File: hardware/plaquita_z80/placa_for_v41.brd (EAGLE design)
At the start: 37.1 x 30.4 mm, 8 parts, among them IC2 REG1117

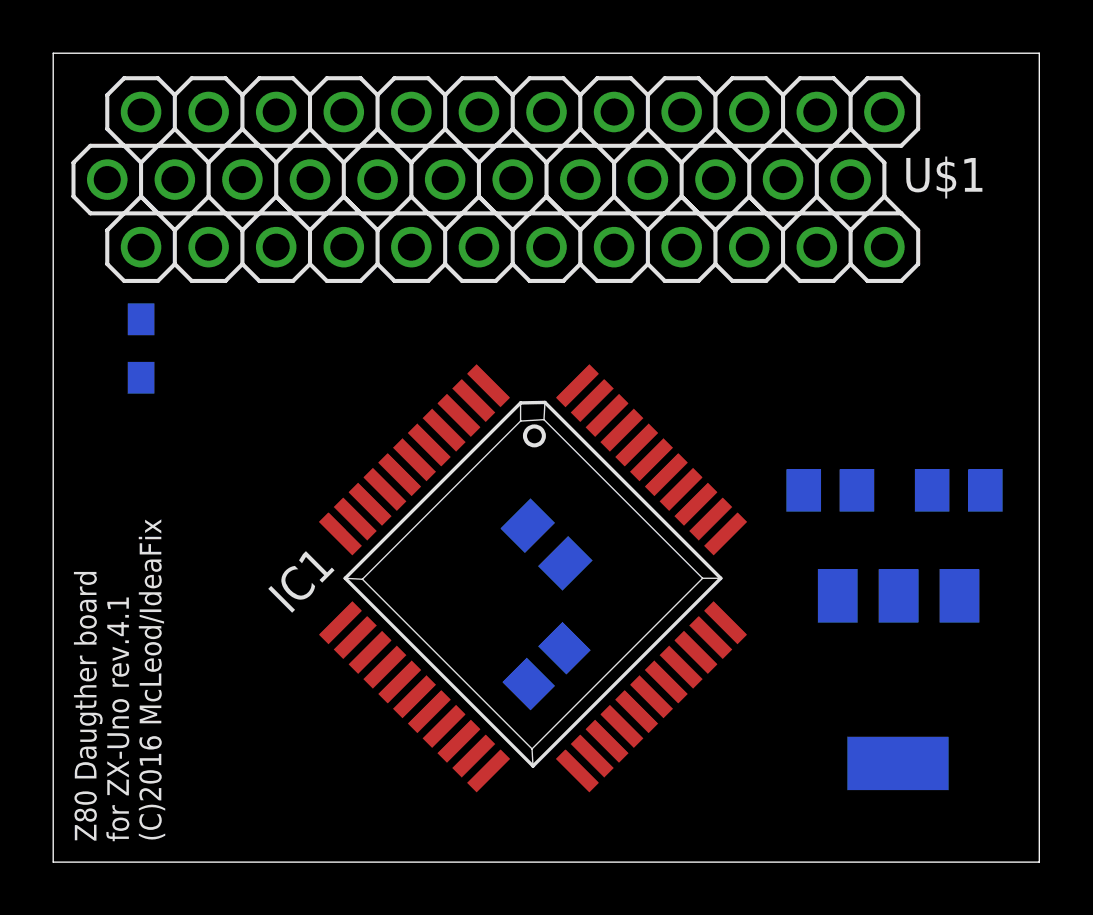
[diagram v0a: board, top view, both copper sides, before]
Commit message: 
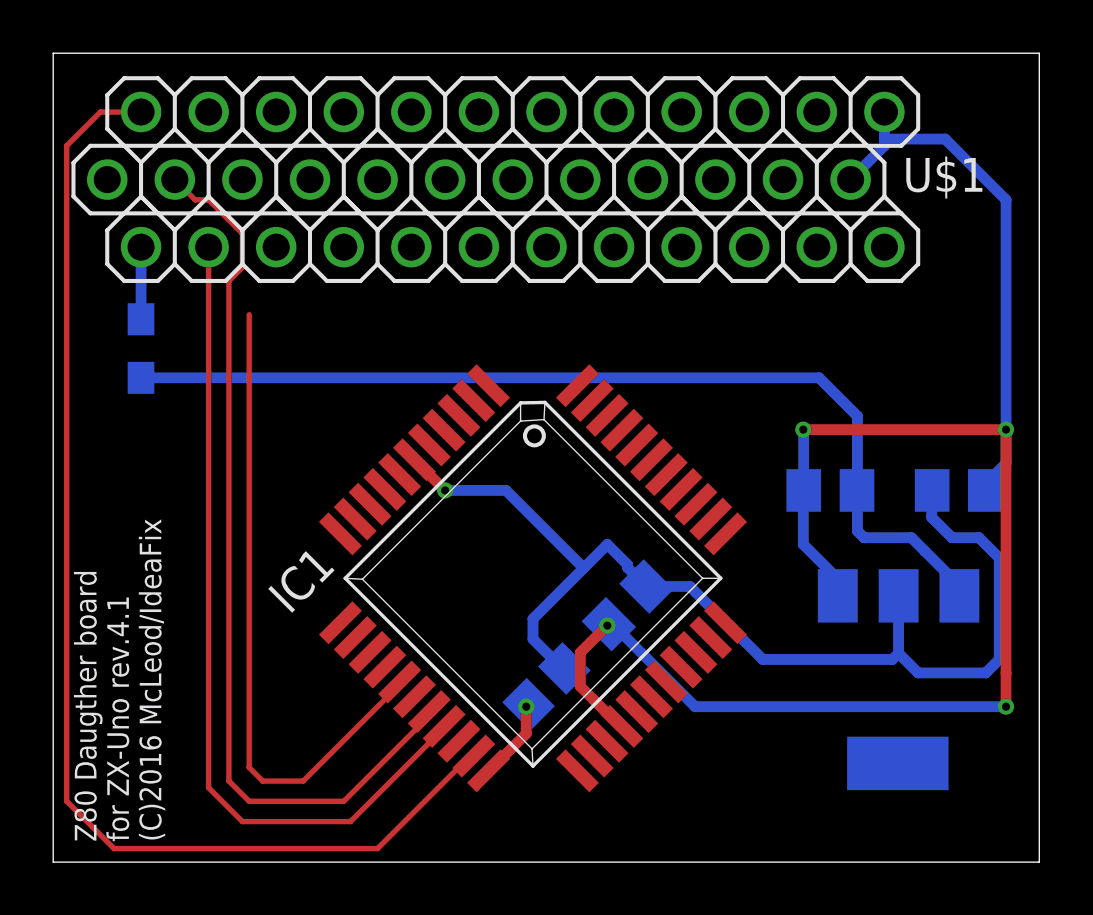
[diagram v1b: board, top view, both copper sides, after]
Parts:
- moved C1 3.81 mm to (21.6, 9.65), turned to 315 degrees
- moved R3 0.76 mm to (18.5, 6.60)
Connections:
- net /IORQ: now also U$1.P9
- net /MREQ: now also U$1.P10
- net /RD: now also U$1.P8
- net /WAIT: now also U$1.P6
- net /WR: now also U$1.P7
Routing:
- net GND: track 0.00 -> 65.8 mm, vias 0 -> 4
- net /WAIT: track 0.00 -> 45.4 mm
- net 3.3V: track 0.00 -> 41.8 mm, vias 0 -> 1
- net +5V: track 0.00 -> 36.9 mm
- net /RD: track 0.00 -> 33.5 mm
- net /WR: track 0.00 -> 31.2 mm
- net /IORQ: track 0.00 -> 24.5 mm
- net /BUSREQ: track 0.00 -> 3.14 mm, vias 0 -> 1
- net N$1: track 0.00 -> 2.71 mm

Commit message: 
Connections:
- net 3.3V renamed VCC
- net /IORQ: now also U$1.P7; no longer U$1.P9
- net /RD: now also U$1.P9; no longer U$1.P8
- net /WR: now also U$1.P8; no longer U$1.P7
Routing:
- net /WR: track 31.2 -> 40.3 mm
- net /IORQ: track 24.5 -> 33.2 mm
- net /RD: track 33.5 -> 40.8 mm
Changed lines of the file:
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@@
 <signal name="/WR">
 <contactref element="IC1" pad="19"/>
-<contactref element="U$1" pad="P7"/>
+<contactref element="U$1" pad="P8"/>
 <wire x1="14.69334375" y1="5.100240625" x2="14.69334375" y2="5.04134375" width="0.2032" layer="1"/>
-<wire x1="14.69334375" y1="5.04134375" x2="11.176" y2="1.524" width="0.2032" layer="1"/>
-<wire x1="11.176" y1="1.524" x2="7.112" y2="1.524" width="0.2032" layer="1"/>
-<wire x1="7.112" y1="1.524" x2="5.842" y2="2.794" width="0.2032" layer="1"/>
-<wire x1="5.842" y1="2.794" x2="5.842" y2="23.114" width="0.2032" layer="1"/>
+<wire x1="14.69334375" y1="5.04134375" x2="10.922" y2="1.27" width="0.2032" layer="1"/>
+<wire x1="10.922" y1="1.27" x2="2.794" y2="1.27" width="0.2032" layer="1"/>
+<wire x1="2.794" y1="1.27" x2="1.27" y2="2.794" width="0.2032" layer="1"/>
+<wire x1="1.27" y1="2.794" x2="1.27" y2="23.114" width="0.2032" layer="1"/>
+<wire x1="1.27" y1="23.114" x2="3.302" y2="25.146" width="0.2032" layer="1"/>
+<wire x1="3.302" y1="25.146" x2="4.064" y2="25.146" width="0.2032" layer="1"/>
+<wire x1="4.064" y1="25.146" x2="4.572" y2="25.654" width="0.2032" layer="1"/>
 </signal>
 <signal name="/RD">
 <contactref element="IC1" pad="18"/>
-<contactref element="U$1" pad="P8"/>
+<contactref element="U$1" pad="P9"/>
 <wire x1="14.13656875" y1="5.657015625" x2="14.13656875" y2="5.50056875" width="0.2032" layer="1"/>
-<wire x1="14.13656875" y1="5.50056875" x2="10.922" y2="2.286" width="0.2032" layer="1"/>
-<wire x1="10.922" y1="2.286" x2="7.366" y2="2.286" width="0.2032" layer="1"/>
-<wire x1="7.366" y1="2.286" x2="6.604" y2="3.048" width="0.2032" layer="1"/>
-<wire x1="6.604" y1="3.048" x2="6.604" y2="21.844" width="0.2032" layer="1"/>
-<wire x1="6.604" y1="21.844" x2="7.112" y2="22.352" width="0.2032" layer="1"/>
-<wire x1="7.112" y1="22.352" x2="7.112" y2="23.622" width="0.2032" layer="1"/>
-<wire x1="7.112" y1="23.622" x2="5.842" y2="24.892" width="0.2032" layer="1"/>
-<wire x1="5.842" y1="24.892" x2="5.334" y2="24.892" width="0.2032" layer="1"/>
-<wire x1="5.334" y1="24.892" x2="4.572" y2="25.654" width="0.2032" layer="1"/>
+<wire x1="14.13656875" y1="5.50056875" x2="10.668" y2="2.032" width="0.2032" layer="1"/>
+<wire x1="10.668" y1="2.032" x2="3.048" y2="2.032" width="0.2032" layer="1"/>
+<wire x1="3.048" y1="2.032" x2="2.032" y2="3.048" width="0.2032" layer="1"/>
+<wire x1="2.032" y1="3.048" x2="2.032" y2="19.812" width="0.2032" layer="1"/>
+<wire x1="2.032" y1="19.812" x2="4.572" y2="22.352" width="0.2032" layer="1"/>
+<wire x1="4.572" y1="22.352" x2="4.572" y2="23.622" width="0.2032" layer="1"/>
+<wire x1="4.572" y1="23.622" x2="5.842" y2="24.892" width="0.2032" layer="1"/>
+<wire x1="5.842" y1="24.892" x2="5.842" y2="28.194" width="0.2032" layer="1"/>
 </signal>
 <signal name="/IORQ">
 <contactref element="IC1" pad="16"/>
-<contactref element="U$1" pad="P9"/>
+<contactref element="U$1" pad="P7"/>
 <wire x1="13.023015625" y1="6.77056875" x2="13.023015625" y2="6.673015625" width="0.2032" layer="1"/>
-<wire x1="13.023015625" y1="6.673015625" x2="9.398" y2="3.048" width="0.2032" layer="1"/>
-<wire x1="9.398" y1="3.048" x2="7.874" y2="3.048" width="0.2032" layer="1"/>
-<wire x1="7.874" y1="3.048" x2="7.366" y2="3.556" width="0.2032" layer="1"/>
-<wire x1="7.366" y1="3.556" x2="7.366" y2="20.574" width="0.2032" layer="1"/>
-<wire x1="7.366" y1="20.574" x2="5.842" y2="28.194" width="0" layer="19" extent="1-16"/>
+<wire x1="13.023015625" y1="6.673015625" x2="9.144" y2="2.794" width="0.2032" layer="1"/>
+<wire x1="9.144" y1="2.794" x2="3.302" y2="2.794" width="0.2032" layer="1"/>
+<wire x1="3.302" y1="2.794" x2="2.794" y2="3.302" width="0.2032" layer="1"/>
+<wire x1="2.794" y1="3.302" x2="2.794" y2="18.796" width="0.2032" layer="1"/>
+<wire x1="2.794" y1="18.796" x2="5.842" y2="21.844" width="0.2032" layer="1"/>
+<wire x1="5.842" y1="21.844" x2="5.842" y2="23.114" width="0.2032" layer="1"/>
 </signal>
 <signal name="/MREQ">
@@
 <wire x1="1.778" y1="28.194" x2="3.302" y2="28.194" width="0.2032" layer="1"/>
 </signal>
-<signal name="3.3V" class="1">
+<signal name="VCC" class="1">
 <contactref element="IC1" pad="6"/>
 <contactref element="C1" pad="1"/>

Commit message: 
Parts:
- renumbered U$1 to CONN_ZXUNO
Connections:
- new net N$10: CONN_ZXUNO.P23
- new net N$11: CONN_ZXUNO.P24
- new net N$12: CONN_ZXUNO.P25
- new net N$13: CONN_ZXUNO.P26
- new net N$9: CONN_ZXUNO.P22
- net /INT: now also CONN_ZXUNO.P12
- net /MREQ: now also CONN_ZXUNO.P11; no longer CONN_ZXUNO.P10
- net /NMI: now also CONN_ZXUNO.P10
- net CLK: now also CONN_ZXUNO.P19
- net D0: now also CONN_ZXUNO.P13
- net D1: now also CONN_ZXUNO.P14
- net D2: now also CONN_ZXUNO.P18
- net D3: now also CONN_ZXUNO.P21
- net D4: now also CONN_ZXUNO.P20
- net D5: now also CONN_ZXUNO.P16
- net D6: now also CONN_ZXUNO.P17
- net D7: now also CONN_ZXUNO.P15
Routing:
- net /MREQ: track 0.00 -> 33.9 mm
- net /INT: track 0.00 -> 32.6 mm, vias 0 -> 1
- net /NMI: track 0.00 -> 28.9 mm
- net D2: track 0.00 -> 17.3 mm
- net D7: track 0.00 -> 15.9 mm, vias 0 -> 1
- net D3: track 0.00 -> 14.8 mm
- net D1: track 0.00 -> 14.7 mm
- net D0: track 0.00 -> 11.8 mm
- net D6: track 0.00 -> 11.5 mm, vias 0 -> 1
- net D4: track 0.00 -> 9.46 mm, vias 0 -> 1
- net D5: track 0.00 -> 8.44 mm
- net CLK: track 0.00 -> 5.36 mm
- net +5V: track 36.9 -> 39.7 mm

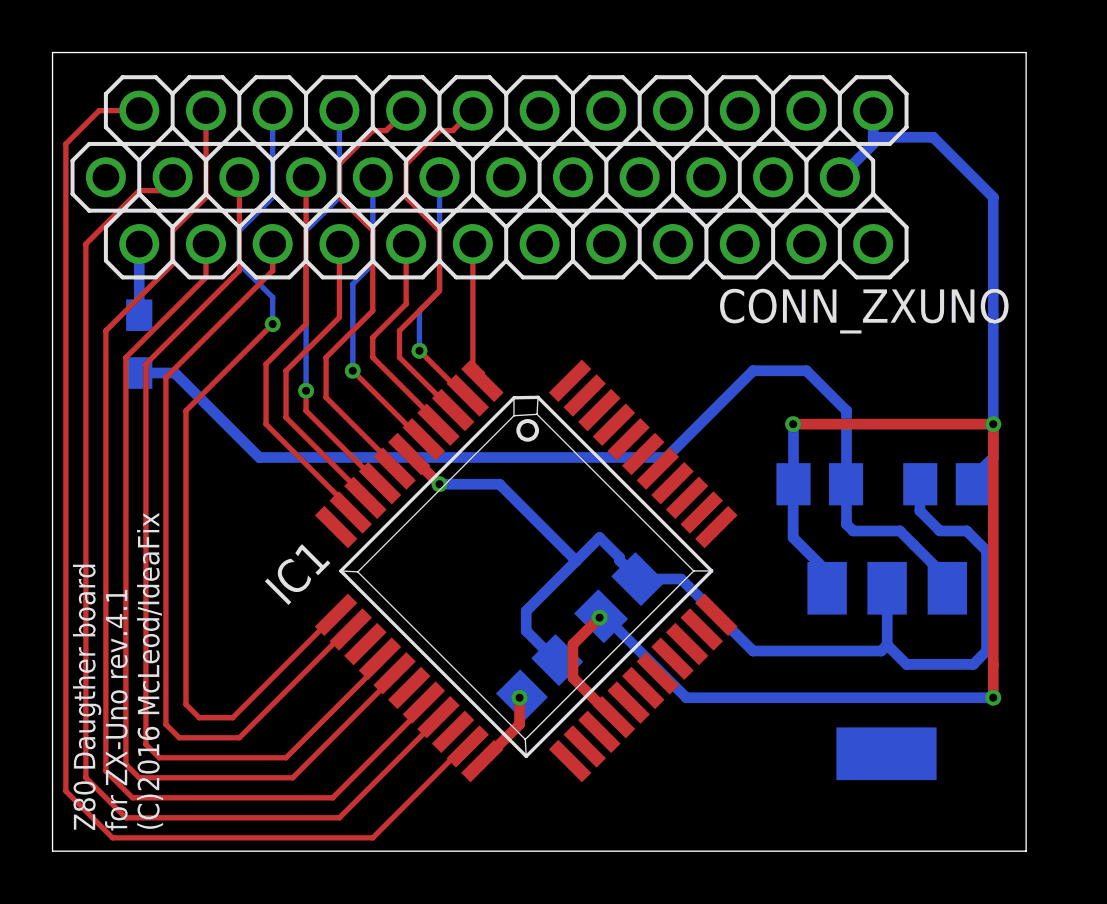
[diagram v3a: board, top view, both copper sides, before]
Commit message: 
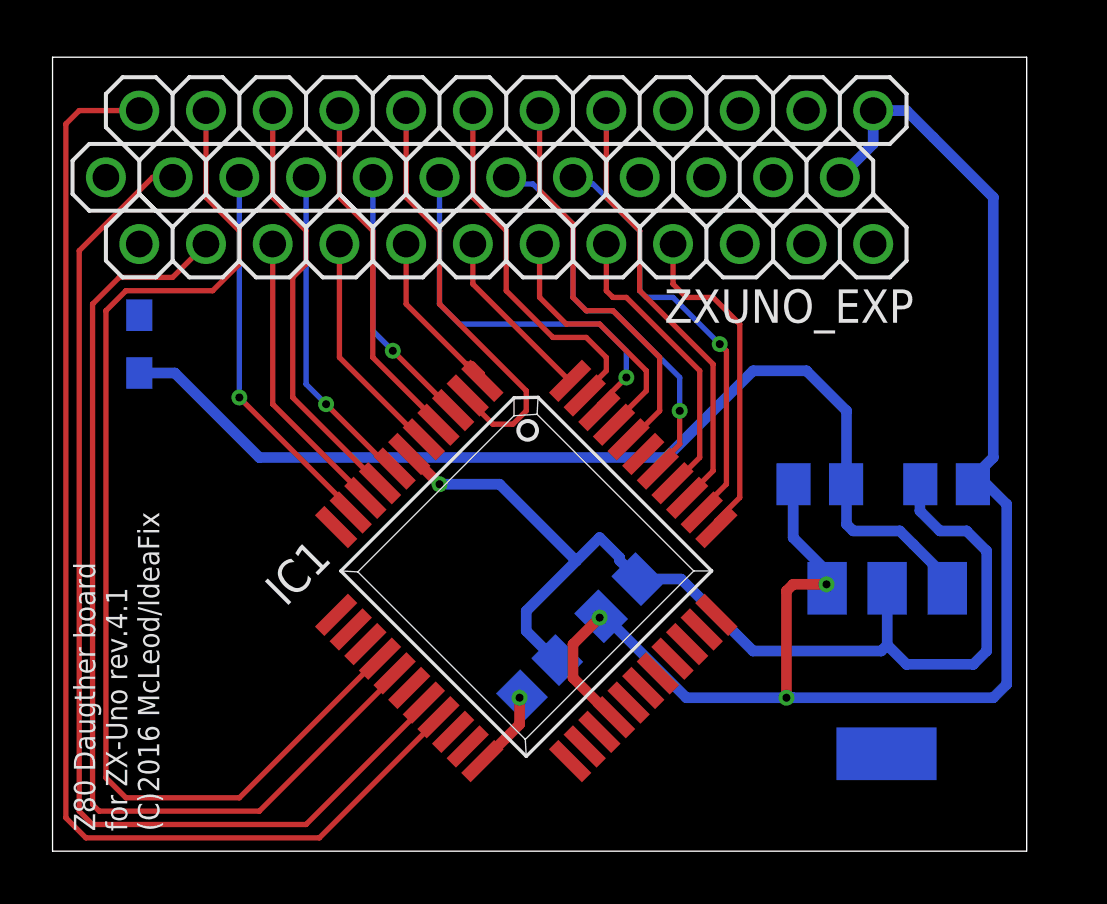
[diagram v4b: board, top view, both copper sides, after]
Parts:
- renumbered CONN_ZXUNO to ZXUNO_EXP
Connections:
- removed net N$10: ZXUNO_EXP.P23
- removed net N$11: ZXUNO_EXP.P24
- removed net N$12: ZXUNO_EXP.P25
- removed net N$13: ZXUNO_EXP.P26
- removed net N$9: ZXUNO_EXP.P22
- new net 3.3V: ZXUNO_EXP.3.3V@1, ZXUNO_EXP.3.3V@2
- new net N$18: ZXUNO_EXP.P29
- new net N$19: ZXUNO_EXP.P30
- new net N$20: ZXUNO_EXP.P31
- new net N$21: ZXUNO_EXP.P32
- new net N$22: ZXUNO_EXP.P33
- net /INT: no longer ZXUNO_EXP.P12
- net /MREQ: now also ZXUNO_EXP.P9; no longer ZXUNO_EXP.P11
- net /NMI: no longer ZXUNO_EXP.P10
- net /RD: now also ZXUNO_EXP.P8; no longer ZXUNO_EXP.P9
- net /WAIT: no longer ZXUNO_EXP.P6
- net /WR: now also ZXUNO_EXP.P6; no longer ZXUNO_EXP.P8
- net A10: now also ZXUNO_EXP.P23
- net A11: now also ZXUNO_EXP.P24
- net A12: now also ZXUNO_EXP.P22
- net A13: now also ZXUNO_EXP.P20
- net A14: now also ZXUNO_EXP.P21
- net A15: now also ZXUNO_EXP.P19
- net A6: now also ZXUNO_EXP.P28
- net A7: now also ZXUNO_EXP.P26
- net A8: now also ZXUNO_EXP.P27
- net A9: now also ZXUNO_EXP.P25
- net CLK: now also ZXUNO_EXP.P16; no longer ZXUNO_EXP.P19
- net D0: now also ZXUNO_EXP.P10; no longer ZXUNO_EXP.P13
- net D1: now also ZXUNO_EXP.P11; no longer ZXUNO_EXP.P14
- net D2: now also ZXUNO_EXP.P14; no longer ZXUNO_EXP.P18
- net D3: now also ZXUNO_EXP.P17; no longer ZXUNO_EXP.P21
- net D4: now also ZXUNO_EXP.P18; no longer ZXUNO_EXP.P20
- net D5: now also ZXUNO_EXP.P15; no longer ZXUNO_EXP.P16
- net D6: now also ZXUNO_EXP.P13; no longer ZXUNO_EXP.P17
- net D7: now also ZXUNO_EXP.P12; no longer ZXUNO_EXP.P15
- net VCC: no longer ZXUNO_EXP.3.3V@1, ZXUNO_EXP.3.3V@2
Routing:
- net /WAIT: track 45.4 -> 0.00 mm
- net /INT: track 32.6 -> 0.00 mm, vias 1 -> 0
- net /NMI: track 28.9 -> 0.00 mm
- net A8: track 0.00 -> 16.8 mm
- net A7: track 0.00 -> 16.5 mm, vias 0 -> 1
- net A11: track 0.00 -> 15.6 mm
- net A13: track 0.00 -> 15.4 mm, vias 0 -> 1
- net A10: track 0.00 -> 15.2 mm, vias 0 -> 1
- net A14: track 0.00 -> 14.0 mm
- net A6: track 0.00 -> 12.8 mm
- net A9: track 0.00 -> 11.3 mm
- net A12: track 0.00 -> 9.82 mm
- net /MREQ: track 33.9 -> 42.9 mm
- net D4: track 9.46 -> 16.5 mm, vias 1 -> 0
- net A15: track 0.00 -> 6.75 mm
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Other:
- board size 37.1 x 30.4 mm -> 37.1 x 30.2 mm

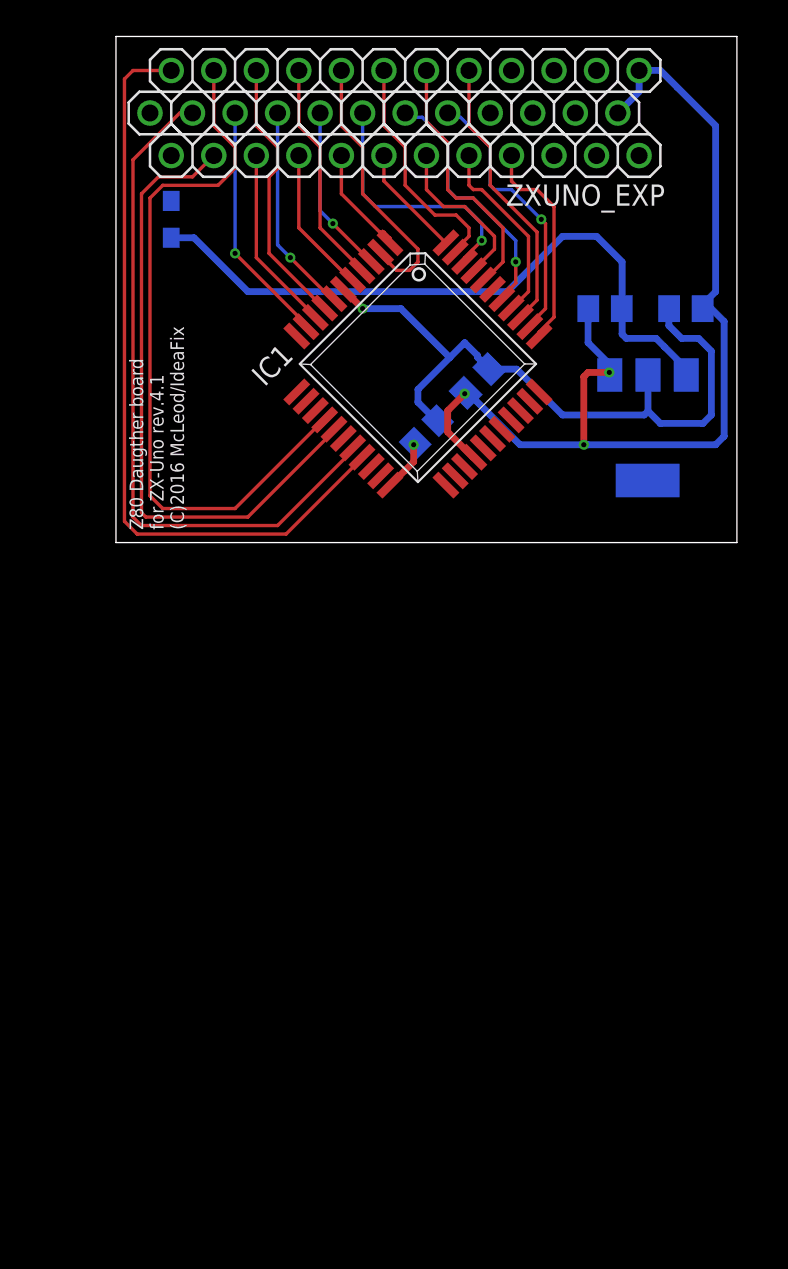
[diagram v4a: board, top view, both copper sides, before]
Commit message: 
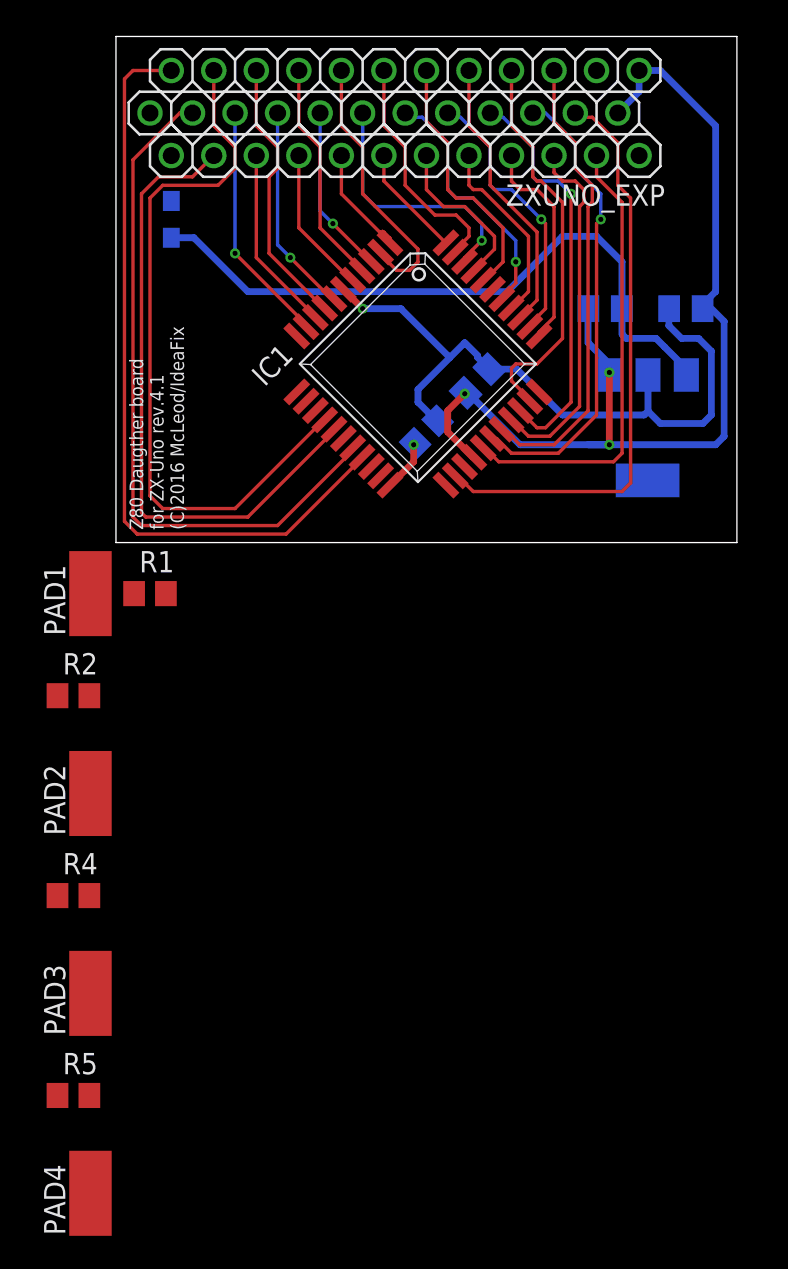
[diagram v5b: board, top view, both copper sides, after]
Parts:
- added PAD1, PAD2, PAD3, PAD4: (no value), wirepad:SMD2,54-5,08
- added R1, R2, R4, R5: 10K, rcl:R0805
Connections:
- removed net N$18: ZXUNO_EXP.P29
- removed net N$19: ZXUNO_EXP.P30
- removed net N$20: ZXUNO_EXP.P31
- removed net N$21: ZXUNO_EXP.P32
- removed net N$22: ZXUNO_EXP.P33
- new net /HALT: IC1.14
- new net /RFSH: IC1.25
- new net /WAIT1: PAD2.1, R2.1
- new net /WAIT2: PAD3.1, R4.1
- new net /WAIT3: PAD4.1, R5.1
- net /M1: now also ZXUNO_EXP.P35
- net /WAIT: now also PAD1.1, R1.1
- net A0: now also ZXUNO_EXP.P34
- net A1: now also ZXUNO_EXP.P32
- net A2: now also ZXUNO_EXP.P33
- net A3: now also ZXUNO_EXP.P31
- net A4: now also ZXUNO_EXP.P29
- net A5: now also ZXUNO_EXP.P30
- net VCC: now also R1.2, R2.2, R4.2, R5.2
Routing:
- net /M1: track 0.00 -> 35.0 mm
- net A1: track 0.00 -> 27.8 mm, vias 0 -> 1
- net A2: track 0.00 -> 27.7 mm
- net A0: track 0.00 -> 27.3 mm
- net A4: track 0.00 -> 24.4 mm, vias 0 -> 1
- net A5: track 0.00 -> 23.6 mm
- net A3: track 0.00 -> 21.5 mm
